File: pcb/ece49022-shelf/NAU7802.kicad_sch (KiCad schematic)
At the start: 10 parts, among them IC1 NAU7802

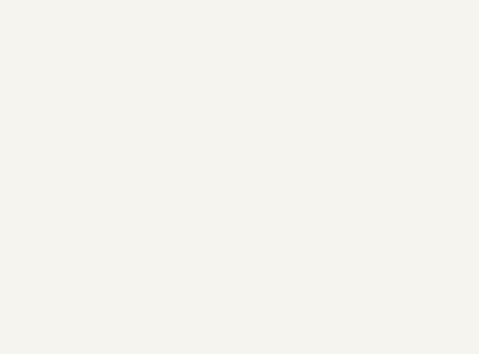
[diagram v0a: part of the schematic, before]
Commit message: connecting top level
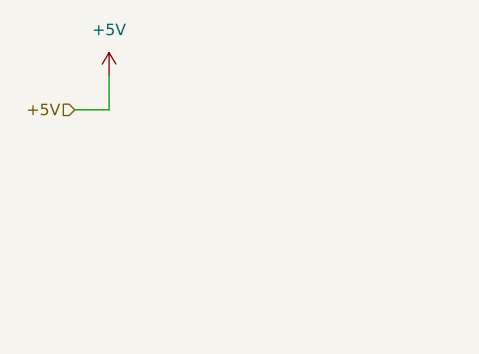
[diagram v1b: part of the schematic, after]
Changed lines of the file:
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@@
+	(wire
+		(pts
+			(xy 41.91 66.04) (xy 45.72 66.04)
+		)
+		(stroke
+			(width 0)
+			(type default)
+		)
+	)
 	(wire
 		(pts
@@
 			(width 0.1524)
 			(type solid)
+		)
+	)
+	(wire
+		(pts
+			(xy 45.72 62.23) (xy 45.72 66.04)
+		)
+		(stroke
+			(width 0)
+			(type default)
 		)
 	)
@@
 		)
 	)
+	(hierarchical_label "+5V"
+		(shape input)
+		(at 41.91 66.04 180)
+		(effects
+			(font
+				(size 1.27 1.27)
+			)
+			(justify right)
+		)
+	)
 	(hierarchical_label "Green"
 		(shape input)
@@
 		)
 	)
+	(symbol
+		(lib_id "power:+5V")
+		(at 45.72 62.23 0)
+		(unit 1)
+		(exclude_from_sim no)
+		(in_bom yes)
+		(on_board yes)
+		(dnp no)
+		(fields_autoplaced yes)
+		(property "Reference" "#PWR026"
+			(at 45.72 66.04 0)
+			(effects
+				(font
+					(size 1.27 1.27)
+				)
+				(hide yes)
+			)
+		)
+		(property "Value" "+5V"
+			(at 45.72 57.15 0)
+			(effects
+				(font
+					(size 1.27 1.27)
+				)
+			)
+		)
+		(property "Footprint" ""
+			(at 45.72 62.23 0)
+			(effects
+				(font
+					(size 1.27 1.27)
+				)
+				(hide yes)
+			)
+		)
+		(property "Datasheet" ""
+			(at 45.72 62.23 0)
+			(effects
+				(font
+					(size 1.27 1.27)
+				)
+				(hide yes)
+			)
+		)
+		(property "Description" "Power symbol creates a global label with name \"+5V\""
+			(at 45.72 62.23 0)
+			(effects
+				(font
+					(size 1.27 1.27)
+				)
+				(hide yes)
+			)
+		)
+		(pin "1"
+		)
+		(instances
+			(project ""
+				(path "/cb6cb1b4-c151-4aa2-8cd7-5430288cfa02/fb213d7f-28bb-4d6d-ba03-4017b4d07db5"
+					(reference "#PWR026")
+					(unit 1)
+				)
+			)
+		)
+	)
